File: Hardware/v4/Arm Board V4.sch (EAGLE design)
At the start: 51 parts, among them IC3 L6206D, U1 SN74LS241DW, U2 XBEE-1B3, U3 LSM9DS0

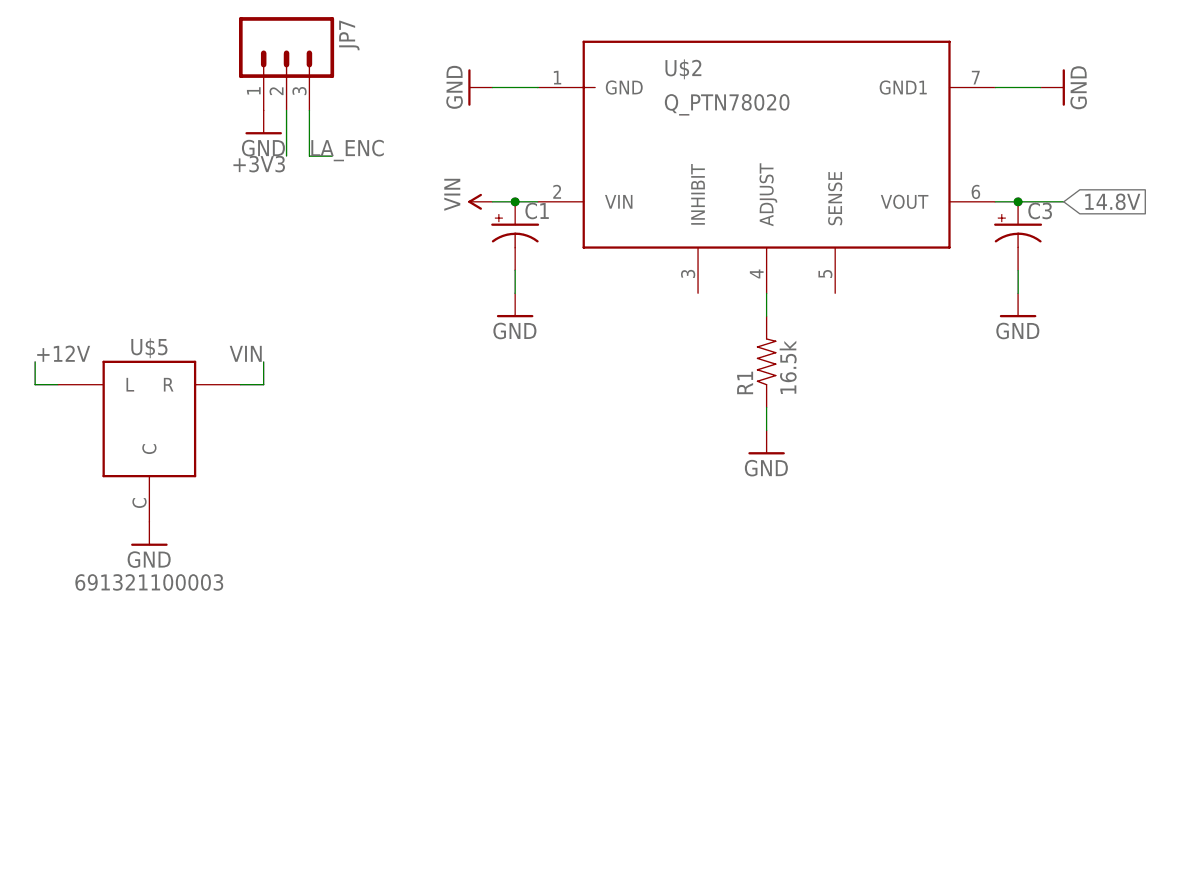
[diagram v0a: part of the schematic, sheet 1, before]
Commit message: Replaced caps on voltage regulator
Need to be moved into place on full eagle and cleaned up a little.  But
replaced them with ones that can be purchased rather then imaginary
ones I wished existed.
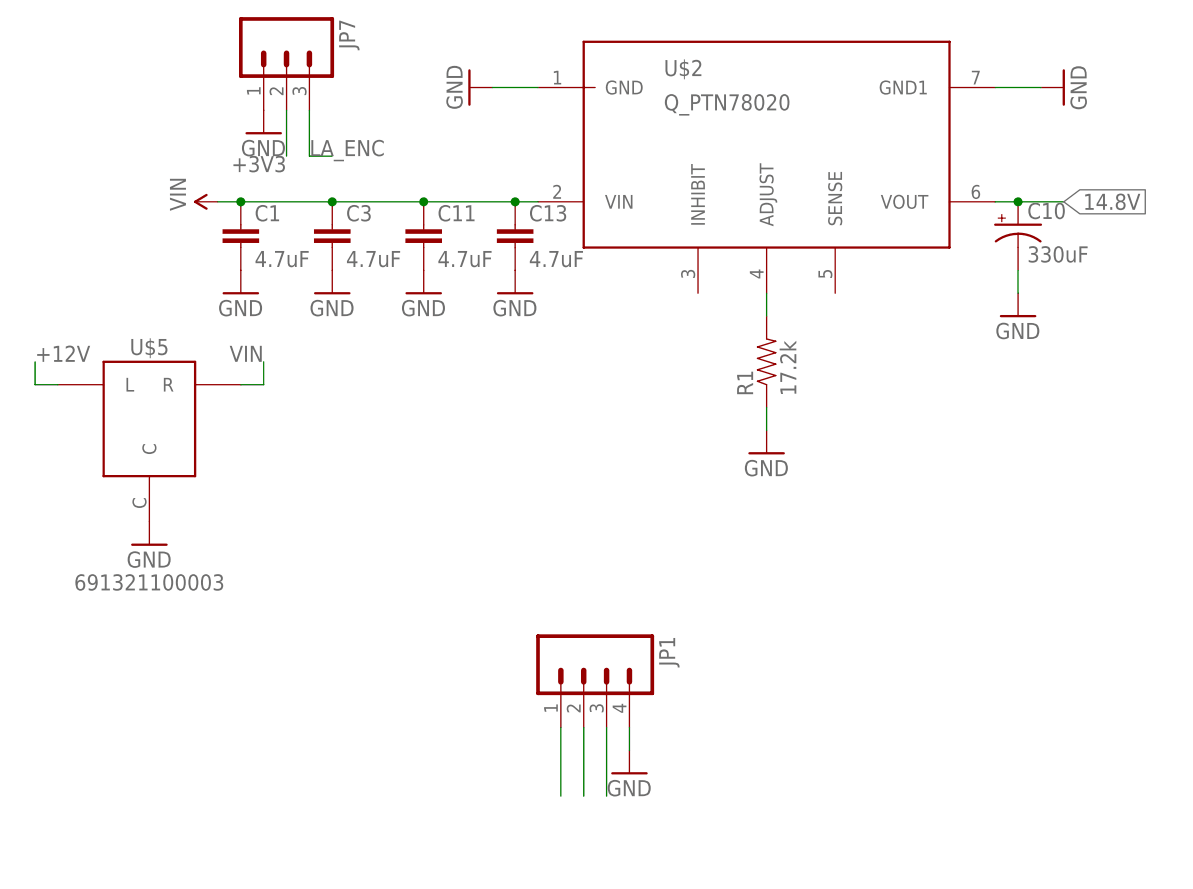
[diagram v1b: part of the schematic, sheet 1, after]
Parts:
- added C10: 330uF, SparkFun-Capacitors:CAP_POLE
- added C11, C13: 4.7uF, SparkFun-Capacitors:CAP1206
- added JP1: (no value), SparkFun-Connectors:M04POLAR
- C1, C3: value (none) -> 4.7uF; device SparkFun-Passives:CAP_POLC -> SparkFun-Capacitors:CAP1206
- R1: value 16.5k -> 17.2k
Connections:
- net +5V: now also JP1.3
- net 14.8V: now also C10.+; no longer C3.+
- net GND: now also C1.2, C10.-, C11.2, C13.2, C3.2, JP1.4; no longer C1.-, C3.-
- net RX_3: now also JP1.2
- net TX_3: now also JP1.1
- net VIN: now also C1.1, C11.1, C13.1, C3.1; no longer C1.+
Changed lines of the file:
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@@
 <part name="U1" library="74LS241" deviceset="SN74LS241DW" device=""/>
 <part name="GND18" library="SparkFun-Aesthetics" deviceset="GND" device=""/>
-<part name="R1" library="SparkFun-Passives" deviceset="RESISTOR" device="1206" value="16.5k"/>
+<part name="R1" library="SparkFun-Passives" deviceset="RESISTOR" device="1206" value="17.2k"/>
 <part name="GND19" library="SparkFun-Aesthetics" deviceset="GND" device=""/>
-<part name="GND20" library="SparkFun-Aesthetics" deviceset="GND" device=""/>
 <part name="GND21" library="SparkFun-Aesthetics" deviceset="GND" device=""/>
-<part name="C3" library="SparkFun-Passives" deviceset="CAP_POL" device="C"/>
 <part name="U$4" library="MAX3077" deviceset="MAX3077" device=""/>
 <part name="U3" library="SparkFun-DigitalIC" deviceset="LSM9DS0" device=""/>
@@
 <part name="C9" library="SparkFun-Passives" deviceset="CAP" device="1206" value="10nF"/>
 <part name="R15" library="SparkFun-Resistors" deviceset="RESISTOR" device="1206" value="100"/>
-<part name="C1" library="SparkFun-Passives" deviceset="CAP_POL" device="C"/>
+<part name="JP1" library="SparkFun-Connectors" deviceset="M04" device="POLAR"/>
+<part name="GND6" library="SparkFun-Aesthetics" deviceset="GND" device=""/>
+<part name="C10" library="SparkFun-Capacitors" deviceset="CAP_POL" device="E" value="330uF"/>
+<part name="C1" library="SparkFun-Capacitors" deviceset="CAP" device="1206" value="4.7uF"/>
+<part name="GND20" library="SparkFun-Aesthetics" deviceset="GND" device=""/>
+<part name="C3" library="SparkFun-Capacitors" deviceset="CAP" device="1206" value="4.7uF"/>
+<part name="C11" library="SparkFun-Capacitors" deviceset="CAP" device="1206" value="4.7uF"/>
+<part name="C13" library="SparkFun-Capacitors" deviceset="CAP" device="1206" value="4.7uF"/>
+<part name="GND22" library="SparkFun-Aesthetics" deviceset="GND" device=""/>
+<part name="GND24" library="SparkFun-Aesthetics" deviceset="GND" device=""/>
+<part name="GND29" library="SparkFun-Aesthetics" deviceset="GND" device=""/>
 </parts>
 <sheets>
@@
 <instance part="GND15" gate="1" x="210.82" y="45.72" rot="R270"/>
 <instance part="GND16" gate="1" x="276.86" y="45.72" rot="R90"/>
-<instance part="SUPPLY2" gate="G$1" x="213.36" y="33.02" rot="R90"/>
+<instance part="SUPPLY2" gate="G$1" x="182.88" y="33.02" rot="R90"/>
 <instance part="U1" gate="A" x="76.2" y="-7.62"/>
 <instance part="GND18" gate="1" x="55.88" y="-30.48" rot="R270"/>
 <instance part="R1" gate="G$1" x="243.84" y="15.24" rot="R90"/>
 <instance part="GND19" gate="1" x="243.84" y="5.08"/>
-<instance part="GND20" gate="1" x="215.9" y="20.32"/>
 <instance part="GND21" gate="1" x="271.78" y="20.32"/>
-<instance part="C3" gate="G$1" x="271.78" y="30.48"/>
 <instance part="R9" gate="G$1" x="15.24" y="-15.24" rot="R90"/>
 <instance part="LED5" gate="G$1" x="15.24" y="-25.4"/>
@@
 <instance part="GND13" gate="1" x="50.8" y="48.26"/>
 <instance part="GND14" gate="1" x="63.5" y="48.26"/>
-<instance part="C1" gate="G$1" x="215.9" y="30.48"/>
+<instance part="JP1" gate="G$1" x="223.52" y="-20.32" rot="R270"/>
+<instance part="GND6" gate="1" x="228.6" y="-30.48"/>
+<instance part="C10" gate="G$1" x="271.78" y="30.48"/>
+<instance part="C1" gate="G$1" x="185.42" y="27.94"/>
+<instance part="GND20" gate="1" x="185.42" y="22.86"/>
+<instance part="C3" gate="G$1" x="195.58" y="27.94"/>
+<instance part="C11" gate="G$1" x="205.74" y="27.94"/>
+<instance part="C13" gate="G$1" x="215.9" y="27.94"/>
+<instance part="GND22" gate="1" x="195.58" y="22.86"/>
+<instance part="GND24" gate="1" x="205.74" y="22.86"/>
+<instance part="GND29" gate="1" x="215.9" y="22.86"/>
 </instances>
 <busses>
@@
 </segment>
 <segment>
-<pinref part="GND20" gate="1" pin="GND"/>
-<wire x1="215.9" y1="22.86" x2="215.9" y2="25.4" width="0.1524" layer="91"/>
-<pinref part="C1" gate="G$1" pin="-"/>
-</segment>
-<segment>
 <pinref part="GND21" gate="1" pin="GND"/>
 <wire x1="271.78" y1="22.86" x2="271.78" y2="25.4" width="0.1524" layer="91"/>
-<pinref part="C3" gate="G$1" pin="-"/>
+<pinref part="C10" gate="G$1" pin="-"/>
 </segment>
 <segment>
@@
 <pinref part="S4" gate="G$1" pin="P$1"/>
 <pinref part="GND14" gate="1" pin="GND"/>
+</segment>
+<segment>
+<pinref part="JP1" gate="G$1" pin="4"/>
+<pinref part="GND6" gate="1" pin="GND"/>
+<wire x1="228.6" y1="-25.4" x2="228.6" y2="-27.94" width="0.1524" layer="91"/>
+</segment>
+<segment>
+<pinref part="C1" gate="G$1" pin="2"/>
+<pinref part="GND20" gate="1" pin="GND"/>
+</segment>
+<segment>
+<pinref part="C3" gate="G$1" pin="2"/>
+<pinref part="GND22" gate="1" pin="GND"/>
+</segment>
+<segment>
+<pinref part="C11" gate="G$1" pin="2"/>
+<pinref part="GND24" gate="1" pin="GND"/>
+</segment>
+<segment>
+<pinref part="C13" gate="G$1" pin="2"/>
+<pinref part="GND29" gate="1" pin="GND"/>
 </segment>
 </net>
@@
 <label x="50.8" y="7.62" size="1.778" layer="95"/>
 </segment>
+<segment>
+<wire x1="226.06" y1="-25.4" x2="226.06" y2="-33.02" width="0.1524" layer="91"/>
+<pinref part="JP1" gate="G$1" pin="3"/>
+</segment>
 </net>
 <net name="14.8V" class="0">
@@
 <segment>
 <pinref part="U$2" gate="G$1" pin="VOUT"/>
+<label x="276.86" y="33.02" size="1.778" layer="95" xref="yes"/>
 <wire x1="269.24" y1="33.02" x2="271.78" y2="33.02" width="0.1524" layer="91"/>
-<pinref part="C3" gate="G$1" pin="+"/>
+<pinref part="C10" gate="G$1" pin="+"/>
 <wire x1="271.78" y1="33.02" x2="276.86" y2="33.02" width="0.1524" layer="91"/>
 <junction x="271.78" y="33.02"/>
-<label x="276.86" y="33.02" size="1.778" layer="95" xref="yes"/>
 </segment>
 <segment>
@@
 <pinref part="U$2" gate="G$1" pin="VIN"/>
 <pinref part="SUPPLY2" gate="G$1" pin="VIN"/>
-<wire x1="215.9" y1="33.02" x2="213.36" y2="33.02" width="0.1524" layer="91"/>
-<pinref part="C1" gate="G$1" pin="+"/>
+<wire x1="182.88" y1="33.02" x2="185.42" y2="33.02" width="0.1524" layer="91"/>
+<pinref part="C1" gate="G$1" pin="1"/>
+<wire x1="185.42" y1="33.02" x2="195.58" y2="33.02" width="0.1524" layer="91"/>
+<pinref part="C3" gate="G$1" pin="1"/>
+<wire x1="195.58" y1="33.02" x2="205.74" y2="33.02" width="0.1524" layer="91"/>
+<junction x="195.58" y="33.02"/>
+<pinref part="C11" gate="G$1" pin="1"/>
+<wire x1="205.74" y1="33.02" x2="215.9" y2="33.02" width="0.1524" layer="91"/>
+<junction x="205.74" y="33.02"/>
+<pinref part="C13" gate="G$1" pin="1"/>
+<wire x1="215.9" y1="33.02" x2="218.44" y2="33.02" width="0.1524" layer="91"/>
 <junction x="215.9" y="33.02"/>
-<wire x1="215.9" y1="33.02" x2="218.44" y2="33.02" width="0.1524" layer="91"/>
+<junction x="185.42" y="33.02"/>
 </segment>
 <segment>
@@
 </segment>
 </net>
+<net name="TX_3" class="0">
+<segment>
+<pinref part="JP1" gate="G$1" pin="1"/>
+<wire x1="220.98" y1="-25.4" x2="220.98" y2="-33.02" width="0.1524" layer="91"/>
+</segment>
+</net>
+<net name="RX_3" class="0">
+<segment>
+<pinref part="JP1" gate="G$1" pin="2"/>
+<wire x1="223.52" y1="-25.4" x2="223.52" y2="-33.02" width="0.1524" layer="91"/>
+</segment>
+</net>

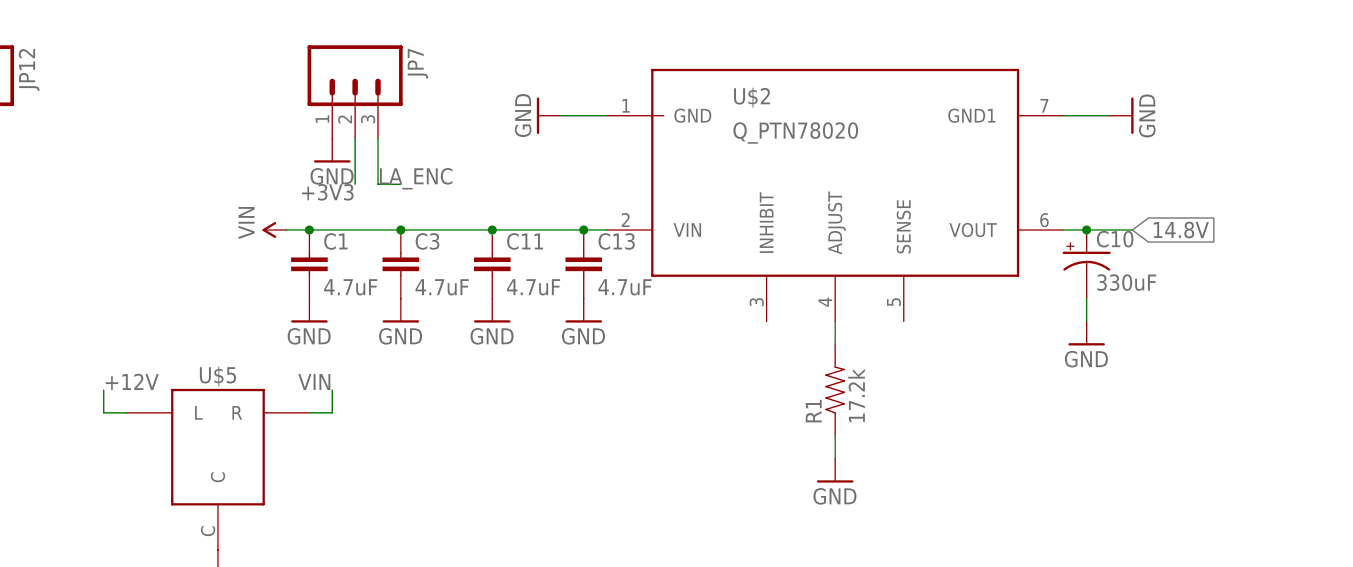
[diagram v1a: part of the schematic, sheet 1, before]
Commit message: Added 1uF ceramic caps to help with ripple
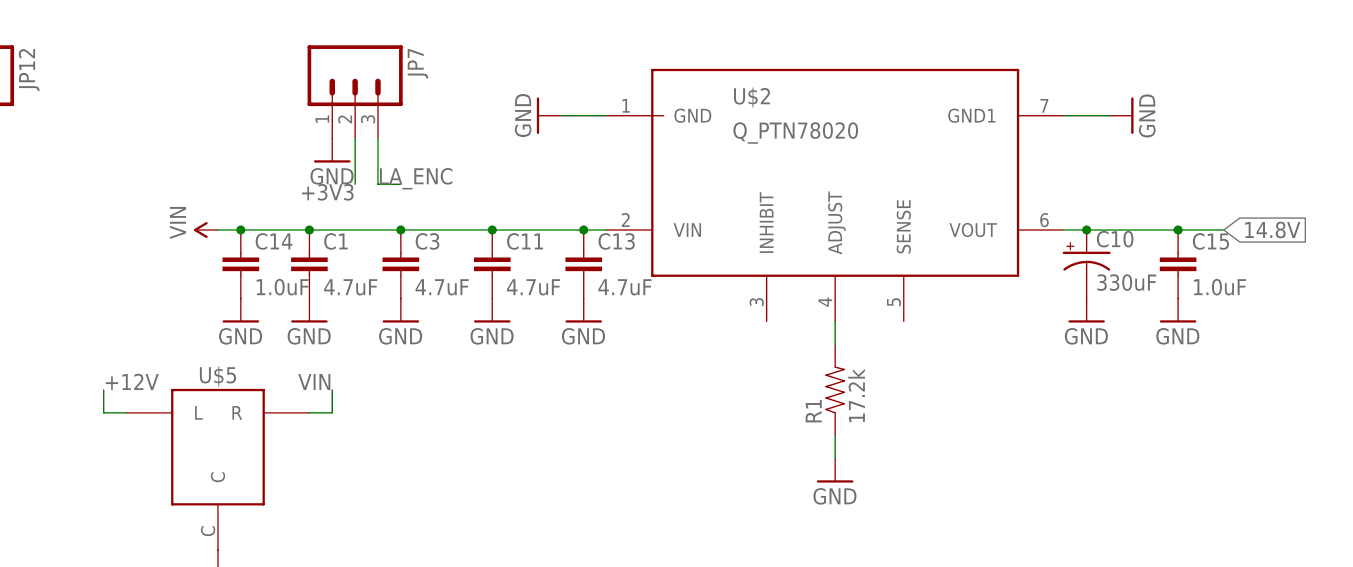
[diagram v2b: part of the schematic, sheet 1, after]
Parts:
- added C14, C15: 1.0uF, SparkFun-Capacitors:1.0UF50V10%(1206)
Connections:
- net 14.8V: now also C15.1
- net GND: now also C14.2, C15.2
- net VIN: now also C14.1
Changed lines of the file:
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@@
 <part name="GND24" library="SparkFun-Aesthetics" deviceset="GND" device=""/>
 <part name="GND29" library="SparkFun-Aesthetics" deviceset="GND" device=""/>
+<part name="C14" library="SparkFun-Capacitors" deviceset="1.0UF50V10%(1206)" device="" value="1.0uF"/>
+<part name="GND31" library="SparkFun-Aesthetics" deviceset="GND" device=""/>
+<part name="C15" library="SparkFun-Capacitors" deviceset="1.0UF50V10%(1206)" device="" value="1.0uF"/>
+<part name="GND32" library="SparkFun-Aesthetics" deviceset="GND" device=""/>
 </parts>
 <sheets>
@@
 <instance part="GND15" gate="1" x="210.82" y="45.72" rot="R270"/>
 <instance part="GND16" gate="1" x="276.86" y="45.72" rot="R90"/>
-<instance part="SUPPLY2" gate="G$1" x="182.88" y="33.02" rot="R90"/>
+<instance part="SUPPLY2" gate="G$1" x="175.26" y="33.02" rot="R90"/>
 <instance part="U1" gate="A" x="76.2" y="-7.62"/>
 <instance part="GND18" gate="1" x="55.88" y="-30.48" rot="R270"/>
 <instance part="R1" gate="G$1" x="243.84" y="15.24" rot="R90"/>
 <instance part="GND19" gate="1" x="243.84" y="5.08"/>
-<instance part="GND21" gate="1" x="271.78" y="20.32"/>
+<instance part="GND21" gate="1" x="271.78" y="22.86"/>
 <instance part="R9" gate="G$1" x="15.24" y="-15.24" rot="R90"/>
 <instance part="LED5" gate="G$1" x="15.24" y="-25.4"/>
@@
 <instance part="GND24" gate="1" x="205.74" y="22.86"/>
 <instance part="GND29" gate="1" x="215.9" y="22.86"/>
+<instance part="C14" gate="G$1" x="177.8" y="27.94"/>
+<instance part="GND31" gate="1" x="177.8" y="22.86"/>
+<instance part="C15" gate="G$1" x="281.94" y="27.94"/>
+<instance part="GND32" gate="1" x="281.94" y="22.86"/>
 </instances>
 <busses>
@@
 <segment>
 <pinref part="GND21" gate="1" pin="GND"/>
-<wire x1="271.78" y1="22.86" x2="271.78" y2="25.4" width="0.1524" layer="91"/>
 <pinref part="C10" gate="G$1" pin="-"/>
 </segment>
@@
 <pinref part="C13" gate="G$1" pin="2"/>
 <pinref part="GND29" gate="1" pin="GND"/>
+</segment>
+<segment>
+<pinref part="C14" gate="G$1" pin="2"/>
+<pinref part="GND31" gate="1" pin="GND"/>
+</segment>
+<segment>
+<pinref part="C15" gate="G$1" pin="2"/>
+<pinref part="GND32" gate="1" pin="GND"/>
 </segment>
 </net>
@@
 <segment>
 <pinref part="U$2" gate="G$1" pin="VOUT"/>
-<label x="276.86" y="33.02" size="1.778" layer="95" xref="yes"/>
+<label x="287.02" y="33.02" size="1.778" layer="95" xref="yes"/>
 <wire x1="269.24" y1="33.02" x2="271.78" y2="33.02" width="0.1524" layer="91"/>
 <pinref part="C10" gate="G$1" pin="+"/>
-<wire x1="271.78" y1="33.02" x2="276.86" y2="33.02" width="0.1524" layer="91"/>
+<wire x1="271.78" y1="33.02" x2="281.94" y2="33.02" width="0.1524" layer="91"/>
 <junction x="271.78" y="33.02"/>
+<pinref part="C15" gate="G$1" pin="1"/>
+<wire x1="281.94" y1="33.02" x2="287.02" y2="33.02" width="0.1524" layer="91"/>
+<junction x="281.94" y="33.02"/>
 </segment>
 <segment>
@@
 <pinref part="U$2" gate="G$1" pin="VIN"/>
 <pinref part="SUPPLY2" gate="G$1" pin="VIN"/>
-<wire x1="182.88" y1="33.02" x2="185.42" y2="33.02" width="0.1524" layer="91"/>
+<wire x1="175.26" y1="33.02" x2="177.8" y2="33.02" width="0.1524" layer="91"/>
 <pinref part="C1" gate="G$1" pin="1"/>
+<wire x1="177.8" y1="33.02" x2="185.42" y2="33.02" width="0.1524" layer="91"/>
 <wire x1="185.42" y1="33.02" x2="195.58" y2="33.02" width="0.1524" layer="91"/>
 <pinref part="C3" gate="G$1" pin="1"/>
@@
 <junction x="215.9" y="33.02"/>
 <junction x="185.42" y="33.02"/>
-</segment>
-<segment>
+<pinref part="C14" gate="G$1" pin="1"/>
+<junction x="177.8" y="33.02"/>
+</segment>
+<segment>
